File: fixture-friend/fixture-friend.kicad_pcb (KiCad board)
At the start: 2 copper layers, 100 x 100 mm, 32 parts, among them J1 10103594-0001LF, J2 TSW-102-07-G-S, U1 NCP1117ST33T3G, U2 W25Q128JVSIQ, U3 RP2040, X1 12MHz

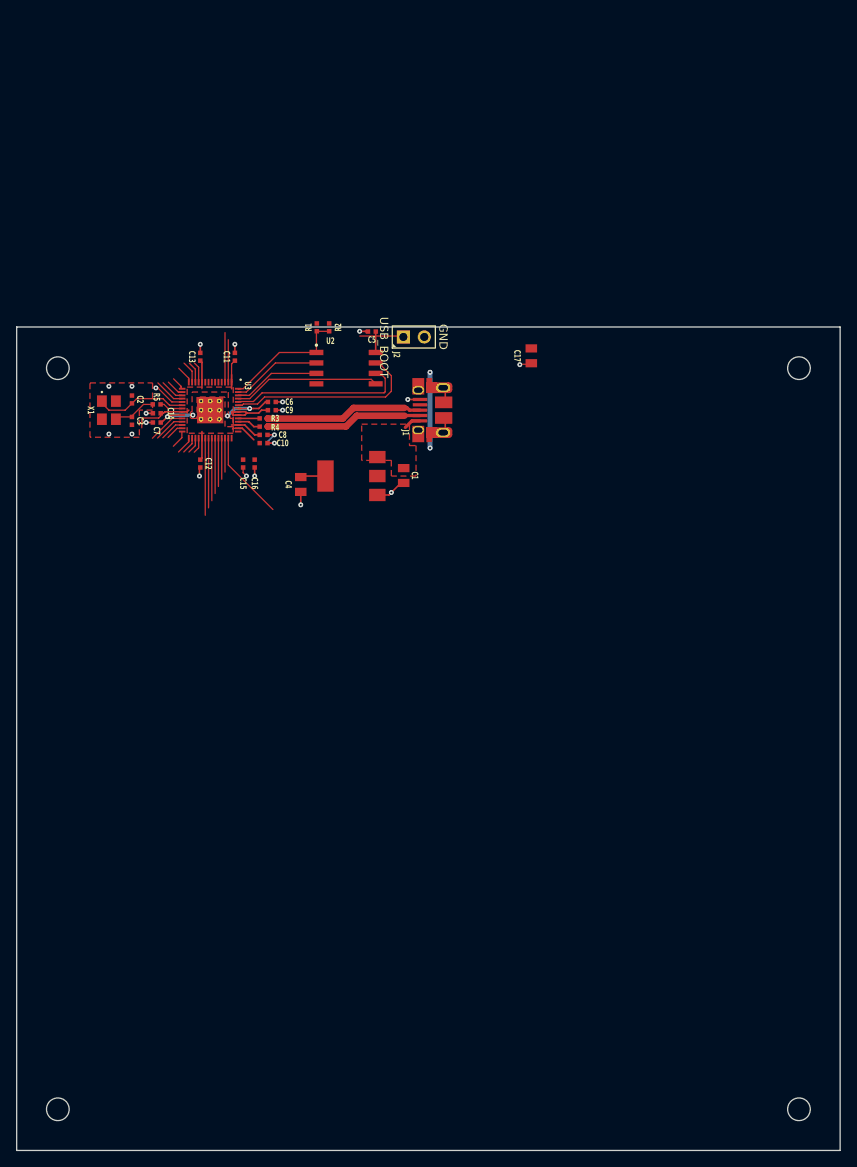
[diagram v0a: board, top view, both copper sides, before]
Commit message: Added modular sub block for the SCH
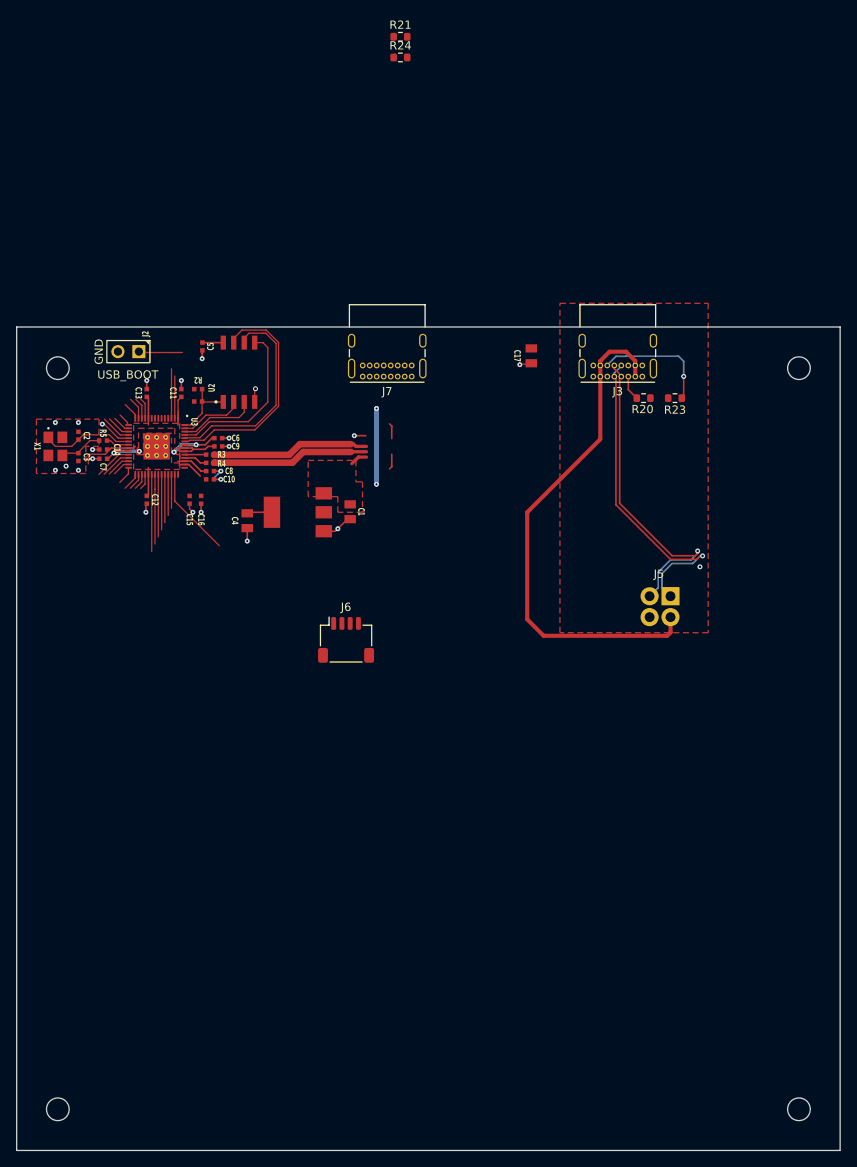
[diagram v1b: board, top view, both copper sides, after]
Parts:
- removed J1: 10103594-0001LF, RPI_COMPILED:amphenol_10103594-0001lf
- added J3: USB_C_Receptacle_USB2.0_16P, Connector_USB:USB_C_Receptacle_GCT_USB4085, F.Cu at (158.5, 78.5)
- added J5: Conn_02x02_Odd_Even, Harwin_P70-2200045:Harwin_P70-2200045_2x02_P2.54mm, F.Cu at (161.9, 105.2)
- added J6: SM04B-SRSS-TB(LF)(SN), Connector_JST:JST_SH_SM04B-SRSS-TB_1x04-1MP_P1.00mm_Horizontal, F.Cu at (122.5, 110.5)
- added J7: USB_C_Receptacle_USB2.0_16P, Connector_USB:USB_C_Receptacle_GCT_USB4085, F.Cu at (130.5, 78.5)
- added R20: 5.1k, Resistor_SMD:R_0603_1608Metric, F.Cu at (158.6, 81.1)
- added R21: 5.1k, Resistor_SMD:R_0603_1608Metric, F.Cu at (129.1, 37.3)
- added R23: 5.1k, Resistor_SMD:R_0603_1608Metric, F.Cu at (162.4, 81.1)
- added R24: 5.1k, Resistor_SMD:R_0603_1608Metric, F.Cu at (129.1, 39.8)
- moved J2 34.7 mm to (96.1, 75.5), turned to 180 degrees
- moved C5 20.7 mm to (105.1, 74.9), turned to -90 degrees
- moved R1 17.6 mm to (104.5, 80.0), turned to 180 degrees
- moved R2 17.0 mm to (104.5, 81.5), turned to 0 degrees
- moved U2 13.0 mm to (109.5, 78.0), turned to 90 degrees
- moved C1 7.85 mm to (123.0, 94.9)
- moved C10 7.85 mm to (106.0, 91.0)
- moved C11 7.85 mm to (102.5, 80.5)
- moved C12 7.85 mm to (98.3, 93.5)
- moved C13 7.85 mm to (98.3, 80.5)
- moved C14 7.85 mm to (93.0, 87.4)
- moved C15 7.85 mm to (103.5, 93.5)
- moved C16 7.85 mm to (104.9, 93.5)
- moved C2 7.85 mm to (90.0, 85.7)
- moved C4 7.85 mm to (110.5, 96.0)
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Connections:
- net /GPIO0 renamed /fixture-friend/GPIO0
- net /GPIO1 renamed /fixture-friend/GPIO1
- net /GPIO10 renamed /fixture-friend/GPIO10
- net /GPIO11 renamed /fixture-friend/GPIO11
- net /GPIO12 renamed /fixture-friend/GPIO12
- net /GPIO13 renamed /fixture-friend/GPIO13
- net /GPIO14 renamed /fixture-friend/GPIO14
- net /GPIO15 renamed /fixture-friend/GPIO15
- net /GPIO16 renamed /fixture-friend/GPIO16
- net /GPIO17 renamed /fixture-friend/GPIO17
- net /GPIO18 renamed /fixture-friend/GPIO18
- net /GPIO19 renamed /fixture-friend/GPIO19
- net /GPIO2 renamed /fixture-friend/GPIO2
- net /GPIO20 renamed /fixture-friend/GPIO20
- net /GPIO21 renamed /fixture-friend/GPIO21
- net /GPIO22 renamed /fixture-friend/GPIO22
- net /GPIO23 renamed /fixture-friend/GPIO23
- net /GPIO24 renamed /fixture-friend/GPIO24
- net /GPIO25 renamed /fixture-friend/GPIO25
- net /GPIO26_ADC0 renamed /fixture-friend/GPIO26_ADC0
- net /GPIO27_ADC1 renamed /fixture-friend/GPIO27_ADC1
- net /GPIO28_ADC2 renamed /fixture-friend/GPIO28_ADC2
- net /GPIO29_ADC3 renamed /fixture-friend/GPIO29_ADC3
- net /GPIO3 renamed /fixture-friend/GPIO3
- net /GPIO4 renamed /fixture-friend/GPIO4
- net /GPIO5 renamed /fixture-friend/GPIO5
- net /GPIO6 renamed /fixture-friend/GPIO6
- net /GPIO7 renamed /fixture-friend/GPIO7
- net /GPIO8 renamed /fixture-friend/GPIO8
- net /GPIO9 renamed /fixture-friend/GPIO9
- net /QSPI_SCLK renamed /fixture-friend/QSPI_SCLK
- net /QSPI_SD0 renamed /fixture-friend/QSPI_SD0
- net /QSPI_SD1 renamed /fixture-friend/QSPI_SD1
- net /QSPI_SD2 renamed /fixture-friend/QSPI_SD2
- net /QSPI_SD3 renamed /fixture-friend/QSPI_SD3
- net /QSPI_SS renamed /fixture-friend/QSPI_SS
- net /RUN renamed /fixture-friend/RUN
- net /SWCLK renamed /fixture-friend/SWCLK
- net /SWD renamed /fixture-friend/SWD
- net /XIN renamed /fixture-friend/XIN
- net /XOUT renamed /fixture-friend/XOUT
- net /~{USB_BOOT} renamed /fixture-friend/~{USB_BOOT}
- R3 pad 1: /USB_D+ -> /fixture-friend/USB_D+
- R4 pad 1: /USB_D- -> /fixture-friend/USB_D-
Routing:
- net /POGO_USB_VBUS: track 0.00 -> 62.4 mm
- net /POGO_USB_D-: track 0.00 -> 40.1 mm, vias 0 -> 1
- net /POGO_USB_D+: track 0.00 -> 39.3 mm, vias 0 -> 1
- net /fixture-friend/USB_D+: track 0.00 -> 19.2 mm
- net /USB_D+: track 19.2 -> 0.00 mm
- net /fixture-friend/USB_D-: track 0.00 -> 19.1 mm
- net /USB_D-: track 19.1 -> 0.00 mm
- net /POGO_USB_CC2: track 0.00 -> 14.6 mm, vias 0 -> 1
- net /fixture-friend/QSPI_SS: track 15.6 -> 8.25 mm
- net /fixture-friend/QSPI_SD3: track 24.3 -> 28.5 mm
- net /fixture-friend/QSPI_SCLK: track 21.4 -> 25.4 mm
- net /fixture-friend/QSPI_SD1: track 10.9 -> 7.69 mm
- net /POGO_USB_CC1: track 0.00 -> 3.04 mm
- net /fixture-friend/QSPI_SD0: track 17.9 -> 20.2 mm
- net GND: track 28.3 -> 30.0 mm, vias 21 -> 24
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- added copper zone on F.Cu, net (none)
- removed copper zone on F.Cu, net +1V1

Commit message: Add RP2040 debug interfaces
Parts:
- added J1: Conn_ARM_JTAG_SWD_10, Connector_PinHeader_1.27mm:PinHeader_2x05_P1.27mm_Vertical_SMD, F.Cu at (106.8, 112.7)
- added J8: 53261-0471, Connector_Molex:Molex_PicoBlade_53261-0471_1x04-1MP_P1.25mm_Horizontal, F.Cu at (107.5, 128.0)
- added J9: SM06B-SRSS-TB(LF)(SN), Connector_JST:JST_SH_SM06B-SRSS-TB_1x06-1MP_P1.00mm_Horizontal, F.Cu at (121.5, 128.0)
- moved R21 44.8 mm to (130.8, 82.0)
- moved R24 38.8 mm to (120.0, 77.5), turned to -90 degrees
- moved C4 32.3 mm to (142.0, 89.0), turned to 0 degrees
- moved U1 27.2 mm to (141.0, 82.8), turned to 180 degrees
- moved C1 25.7 mm to (140.9, 76.5), turned to 0 degrees
- moved C17 7.55 mm to (146.5, 83.4)
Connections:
- U3 pad 11: /fixture-friend/GPIO8 -> /SPI1_MISO
- U3 pad 12: /fixture-friend/GPIO9 -> /SPI1_CS_N
- U3 pad 13: /fixture-friend/GPIO10 -> /SPI1_SCK
- U3 pad 14: /fixture-friend/GPIO11 -> /SPI1_MOSI
- U3 pad 15: /fixture-friend/GPIO12 -> /PROBE_SWCLK
- U3 pad 16: /fixture-friend/GPIO13 -> /PROBE_SWDIO
- U3 pad 17: /fixture-friend/GPIO14 -> /PROBE_SWDIO
- U3 pad 2: /fixture-friend/GPIO0 -> unconnected-(U3-GPIO0-Pad2)
- U3 pad 3: /fixture-friend/GPIO1 -> unconnected-(U3-GPIO1-Pad3)
- U3 pad 6: /fixture-friend/GPIO4 -> /UART1_TX
- U3 pad 7: /fixture-friend/GPIO5 -> /UART1_RX
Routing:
- net /fixture-friend/USB_D-: track 19.1 -> 29.4 mm, vias 0 -> 1
- net +3V3: track 43.8 -> 34.6 mm, vias 2 -> 0
- net /fixture-friend/USB_D+: track 19.2 -> 28.0 mm, vias 0 -> 1
- net /fixture-friend/CC2: track 0.00 -> 7.61 mm
- net unconnected-(U3-GPIO1-Pad3): track 0.00 -> 5.98 mm
- net /fixture-friend/GPIO1: track 5.98 -> 0.00 mm
- net unconnected-(U3-GPIO0-Pad2): track 0.00 -> 5.11 mm
- net /fixture-friend/GPIO0: track 5.11 -> 0.00 mm
- net /PROBE_SWDIO: track 0.00 -> 5.05 mm
- net /fixture-friend/CC1: track 0.00 -> 3.95 mm
- net GND: track 30.0 -> 26.7 mm, vias 24 -> 25
- net /fixture-friend/GPIO14: track 2.91 -> 0.00 mm
- net /fixture-friend/GPIO10: track 2.68 -> 0.00 mm
- net /SPI1_SCK: track 0.00 -> 2.68 mm
- net /fixture-friend/GPIO9: track 2.58 -> 0.00 mm
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- added copper zone on B.Cu, net GND
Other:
- board text added: "I2C"
- board text added: "SPI"
- board text added: "SWD"
- board text added: "Tester"
- board text added: "UART"
- board text added: "USB-C"
